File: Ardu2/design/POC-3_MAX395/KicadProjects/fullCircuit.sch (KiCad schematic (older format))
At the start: 123 parts, among them P1 CONN_01X02, P7 CONN_01X15, U1 Pyboard, U10 MAX395, U11 MAX395, U12 MAX395, U13 MAX395, U14 MAX395, U15 MAX395, U16 MAX395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

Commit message: updates after testing on breadboard - still need reverse polarity protection
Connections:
- net AOut-: now also U17.12 (COM3), U17.13 (COM4), U17.16 (NO5), U17.17 (COM6), U17.8 (COM1)
- net BOut-: now also U14.12 (COM3), U14.13 (COM4), U14.16 (NO5), U14.17 (COM6), U14.8 (COM1)
- net COut-: now also U11.12 (COM3), U11.13 (COM4), U11.16 (NO5), U11.17 (COM6), U11.8 (COM1)
- net DOut-: now also U8.12 (COM3), U8.13 (COM4), U8.16 (NO5), U8.17 (COM6), U8.8 (COM1)
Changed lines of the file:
@@
 Sheet 1 1
 Title "ArduGuitar Full Circuit MAX395"
-Date "Sat 30 May 2015"
-Rev "1.0"
+Date "Sun 31 May 2015"
+Rev "1.2"
 Comp "www.arduguitar.org"
 Comment1 ""
@@
 Text Label 15600 6600 0    60   ~ 0
 BOut+
+Text Label 6450 2100 0    60   ~ 0
+DOut-
+Connection ~ 6450 2100
+Text Label 9750 2100 0    60   ~ 0
+COut-
+Connection ~ 9750 2100
+Text Label 13100 2100 0    60   ~ 0
+BOut-
+Connection ~ 13100 2100
+Text Label 16400 2100 0    60   ~ 0
+AOut-
+Connection ~ 16400 2100
 $EndSCHEMATC

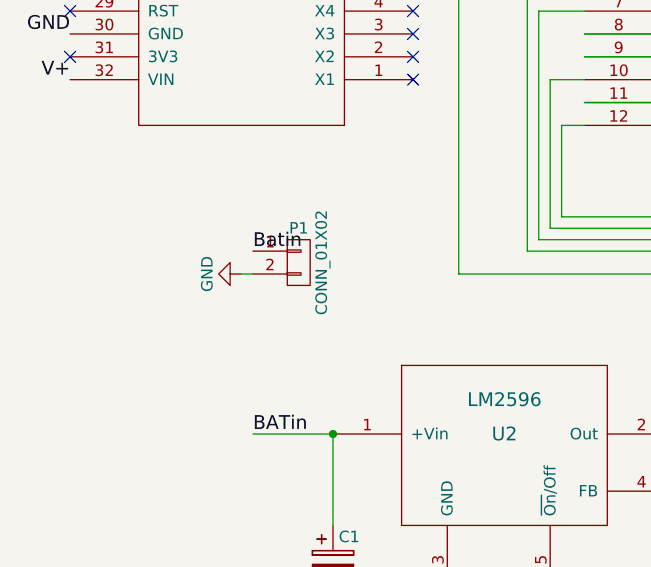
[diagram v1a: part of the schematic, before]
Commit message: reverse polarity added, Cout+ net corrected
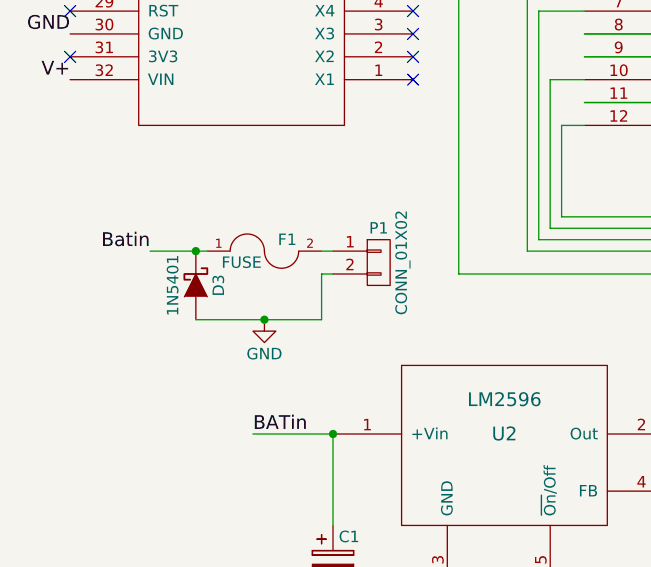
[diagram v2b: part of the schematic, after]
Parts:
- added D3: 1N5401, Diodes_ThroughHole:Diode_DO-201AD_Horizontal_RM15, symbol D_Schottky
- added F1: FUSE, Fuse_Holders_and_Fuses:Fuse_TE5_Littlefuse-395Series, symbol FUSE
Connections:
- net Batin: now also D3.1 (K), F1.1; no longer P1.1 (P1)
- net GND: now also D3.2 (A)
- new net: F1.2, P1.1 (P1)
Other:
- moved on the sheet: P1
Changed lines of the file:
@@
 EELAYER 25 0
 EELAYER END
-$Descr User 19685 9843
+$Descr User 20000 12000
 encoding utf-8
 Sheet 1 1
 Title "ArduGuitar Full Circuit MAX395"
 Date "Sun 31 May 2015"
-Rev "1.2"
+Rev "1.3"
 Comp "www.arduguitar.org"
 Comment1 ""
@@
 L CONN_01X02 P1
 U 1 1 55626D06
-P 1750 5900
-F 0 "P1" H 1750 6050 50  0000 C CNN
-F 1 "CONN_01X02" V 1850 5900 50  0000 C CNN
-F 2 "Connect:PINHEAD1-2" H 1750 5900 60  0001 C CNN
-F 3 "" H 1750 5900 60  0000 C CNN
-	1    1750 5900
+P 2100 5900
+F 0 "P1" H 2100 6050 50  0000 C CNN
+F 1 "CONN_01X02" V 2200 5900 50  0000 C CNN
+F 2 "Connect:PINHEAD1-2" H 2100 5900 60  0001 C CNN
+F 3 "" H 2100 5900 60  0000 C CNN
+	1    2100 5900
 	1    0    0    -1
 $EndComp
@@
 Text Label 14100 7400 0    60   ~ 0
 V-
-Text Label 1550 5850 0    60   ~ 0
+Text Label 1100 5850 2    60   ~ 0
 Batin
 $Comp
 L GND #PWR015
 U 1 1 5564C67C
-P 1500 5950
-F 0 "#PWR015" H 1500 5700 50  0001 C CNN
-F 1 "GND" H 1500 5800 50  0000 C CNN
-F 2 "" H 1500 5950 60  0000 C CNN
-F 3 "" H 1500 5950 60  0000 C CNN
-	1    1500 5950
-	0    1    1    0
+P 1600 6150
+F 0 "#PWR015" H 1600 5900 50  0001 C CNN
+F 1 "GND" H 1600 6000 50  0000 C CNN
+F 2 "" H 1600 6150 60  0000 C CNN
+F 3 "" H 1600 6150 60  0000 C CNN
+	1    1600 6150
+	1    0    0    -1
 $EndComp
 $Comp
@@
 Connection ~ 11600 3100
 Wire Wire Line
-	1500 5950 1550 5950
+	1850 5950 1900 5950
 Connection ~ 9750 2900
 Wire Wire Line
@@
 AOut-
 Connection ~ 16400 2100
+$Comp
+L FUSE F1
+U 1 1 556B808C
+P 1600 5850
+F 0 "F1" H 1700 5900 50  0000 C CNN
+F 1 "FUSE" H 1500 5800 50  0000 C CNN
+F 2 "Fuse_Holders_and_Fuses:Fuse_TE5_Littlefuse-395Series" H 1600 5850 60  0001 C CNN
+F 3 "" H 1600 5850 60  0000 C CNN
+	1    1600 5850
+	1    0    0    -1
+$EndComp
+$Comp
+L D_Schottky D3
+U 1 1 556B811F
+P 1300 6000
+F 0 "D3" H 1300 6100 50  0000 C CNN
+F 1 "1N5401" H 1300 5900 50  0000 C CNN
+F 2 "Diodes_ThroughHole:Diode_DO-201AD_Horizontal_RM15" H 1300 6000 60  0001 C CNN
+F 3 "" H 1300 6000 60  0000 C CNN
+	1    1300 6000
+	0    1    1    0
+$EndComp
+Wire Wire Line
+	1850 6150 1850 5950
+Wire Wire Line
+	1300 6150 1850 6150
+Connection ~ 1600 6150
+Wire Wire Line
+	1100 5850 1350 5850
+Wire Wire Line
+	1900 5850 1850 5850
+Connection ~ 1300 5850
 $EndSCHEMATC
